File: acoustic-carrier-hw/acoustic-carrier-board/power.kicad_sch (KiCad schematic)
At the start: 71 parts, among them J201 Conn_02x06_Odd_Even, Q201 AO3401A, U201 TPS2121RUX, U202 TLV62569DBV, U203 TLV62569DBV, U204 TLV62569DBV, U205 TLV62569DBV, U206 OPA376xxDBV

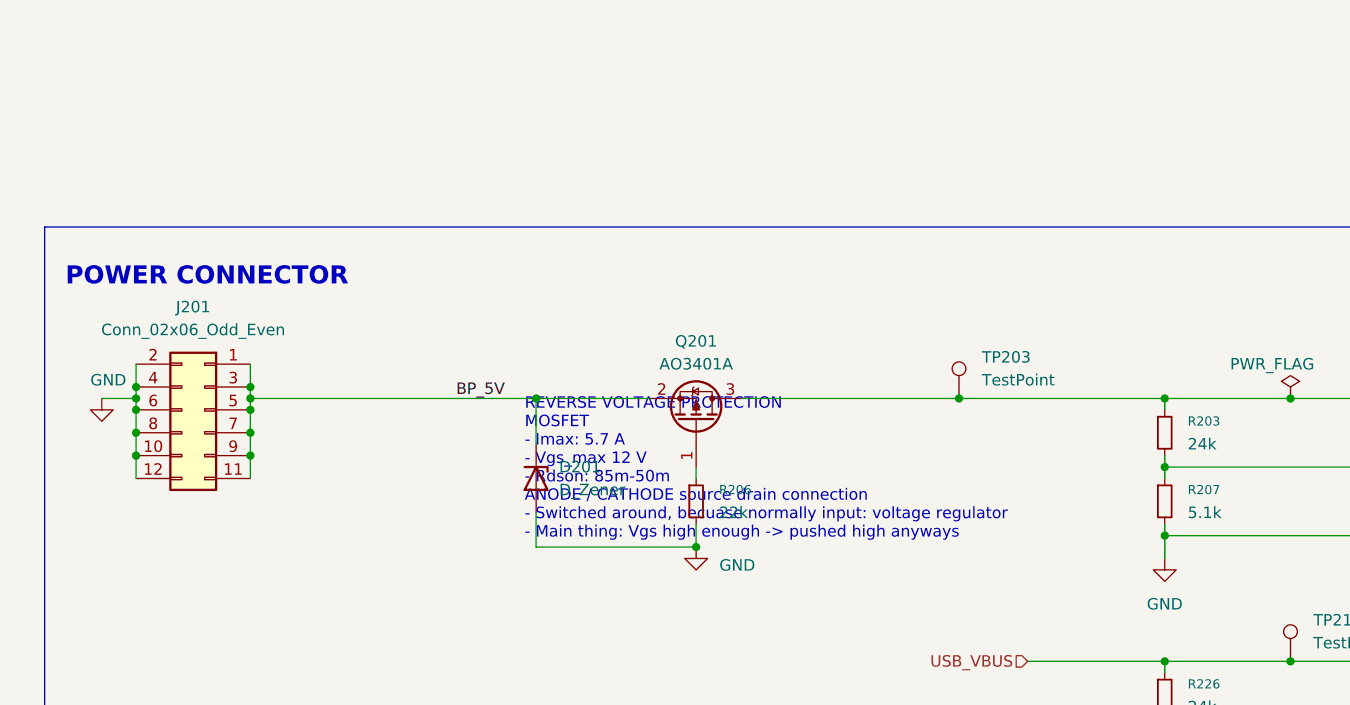
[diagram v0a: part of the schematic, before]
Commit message: [carrier] Routed out signals for board-to-board PTH
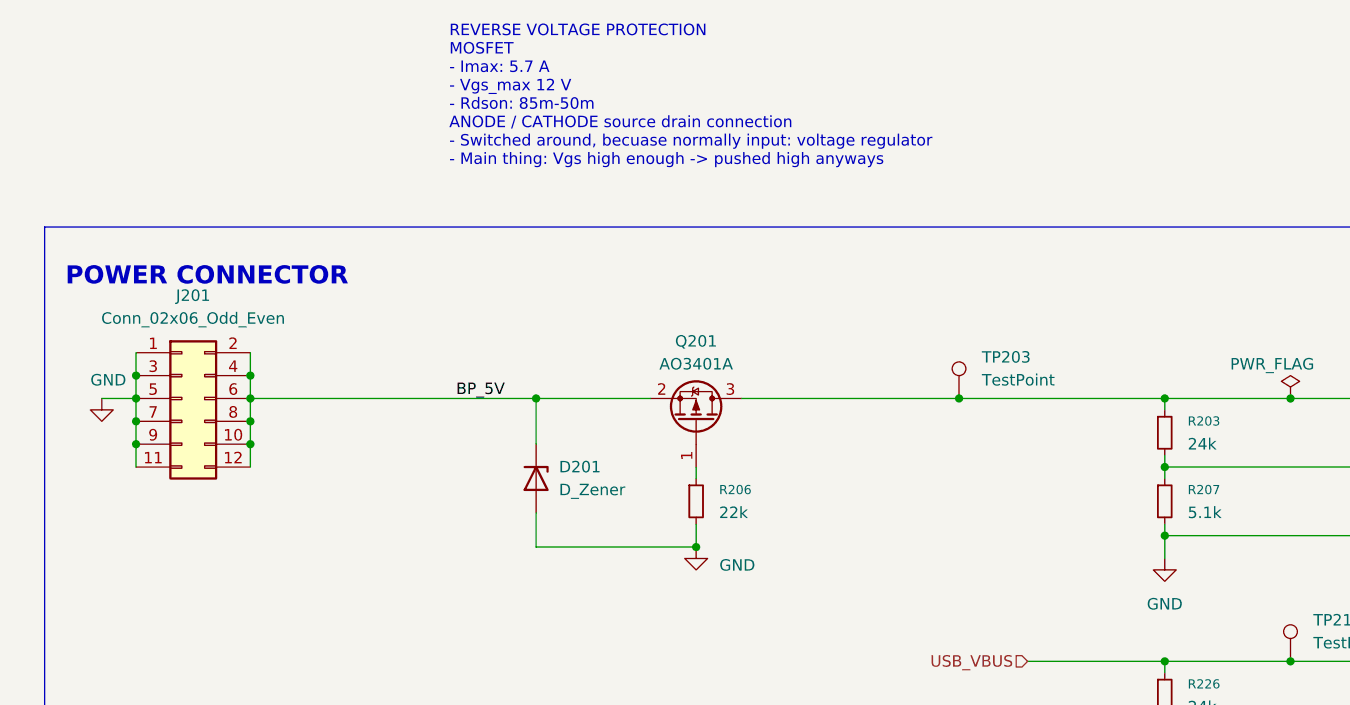
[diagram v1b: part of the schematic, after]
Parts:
- J201: footprint Connector_PinSocket_2.54mm:PinSocket_2x06_P2.54mm_Horizontal -> Connector_PinSocket_2.54mm:PinSocket_2x06_P2.54mm_Vertical; LPN C2897426 -> (none); MPN PM254-2-06-W-8.5 -> (none)
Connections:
- net BP_5V: now also J201.10 (Pin_10), J201.12 (Pin_12), J201.2 (Pin_2), J201.4 (Pin_4), J201.6 (Pin_6), J201.8 (Pin_8); no longer J201.1 (Pin_1), J201.11 (Pin_11), J201.3 (Pin_3), J201.5 (Pin_5), J201.7 (Pin_7), J201.9 (Pin_9)
- net GND: now also J201.1 (Pin_1), J201.11 (Pin_11), J201.3 (Pin_3), J201.5 (Pin_5), J201.7 (Pin_7), J201.9 (Pin_9); no longer J201.10 (Pin_10), J201.12 (Pin_12), J201.2 (Pin_2), J201.4 (Pin_4), J201.6 (Pin_6), J201.8 (Pin_8)

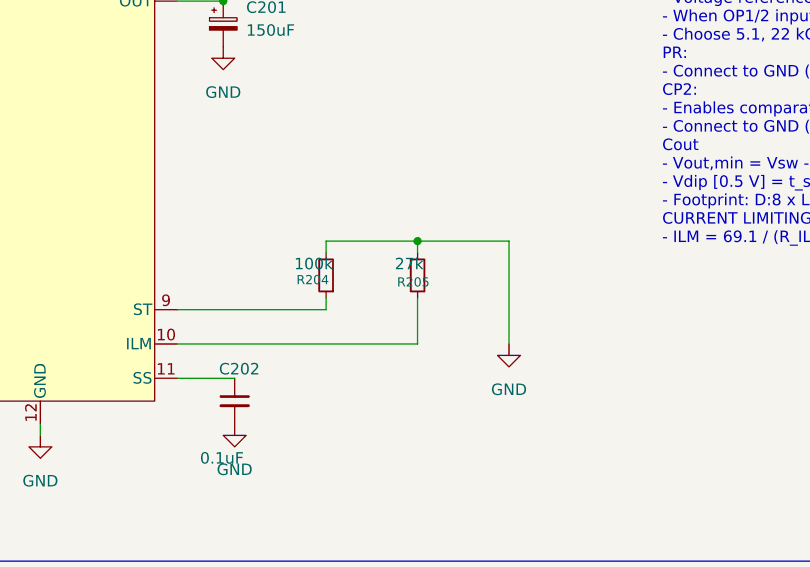
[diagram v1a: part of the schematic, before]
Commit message: [carrier] Changed all vias to (pcheaper) 0.2/0.35 size (next) create basic test-VHDL for clock-signal fanout checks
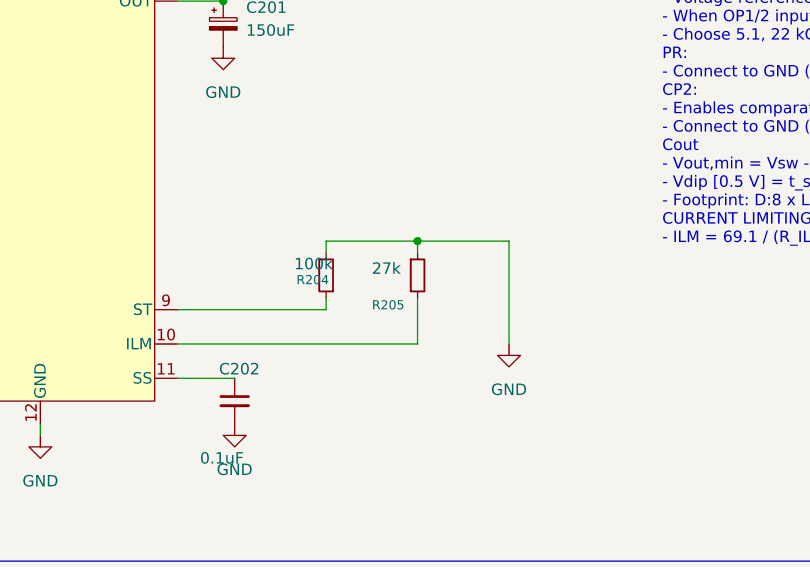
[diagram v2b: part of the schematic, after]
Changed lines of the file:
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@@
 		(dnp no)
 		(property "Reference" "R205"
-			(at 223.774 75.692 0)
+			(at 220.98 78.232 0)
 			(effects
 				(font
@@
 		)
 		(property "Value" "27k"
-			(at 223.52 73.66 0)
+			(at 220.98 74.168 0)
 			(effects
 				(font

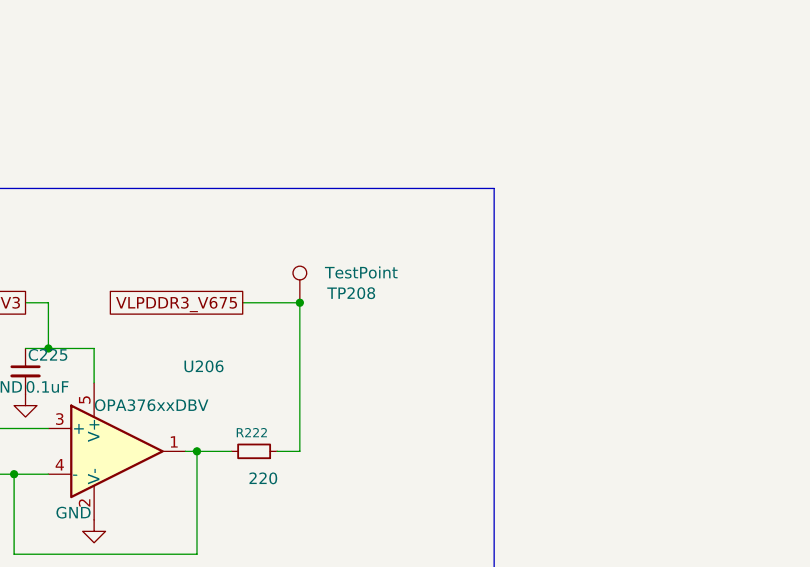
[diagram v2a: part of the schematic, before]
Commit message: [carrier] Added decoupling to LPDDR3 and routed VREF (next) finalize power supply
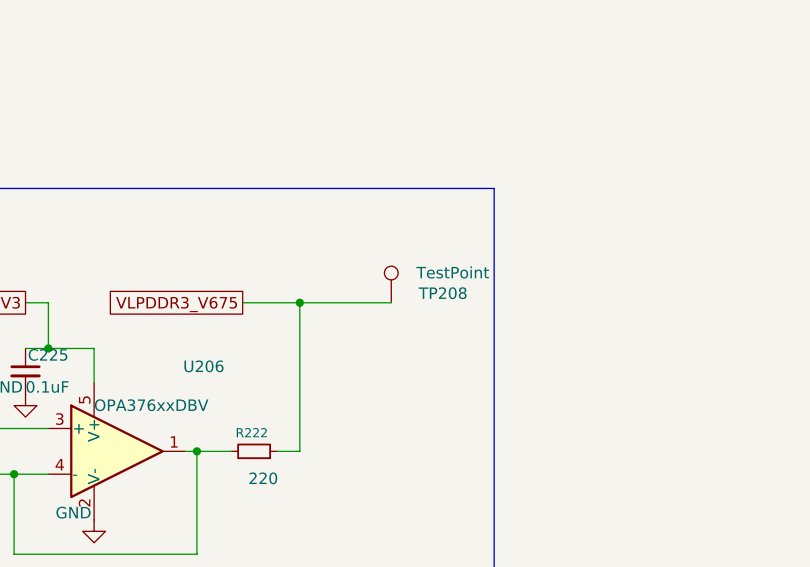
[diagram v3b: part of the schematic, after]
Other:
- moved on the sheet: TP208
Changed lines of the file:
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@@
 	(wire
 		(pts
+			(xy 281.94 237.49) (xy 271.78 237.49)
+		)
+		(stroke
+			(width 0)
+			(type default)
+		)
+	)
+	(wire
+		(pts
 			(xy 215.9 71.12) (xy 215.9 72.39)
 		)
@@
 	(symbol
 		(lib_id "Connector:TestPoint")
-		(at 271.78 237.49 0)
+		(at 281.94 237.49 0)
 		(unit 1)
 		(exclude_from_sim no)
@@
 		(dnp no)
 		(property "Reference" "TP208"
-			(at 274.828 236.474 0)
+			(at 284.988 236.474 0)
 			(effects
 				(font
@@
 		)
 		(property "Value" "TestPoint"
-			(at 274.574 234.188 0)
+			(at 284.734 234.188 0)
 			(effects
 				(font
@@
 		)
 		(property "Footprint" "TestPoint:TestPoint_Loop_D1.80mm_Drill1.0mm_Beaded"
-			(at 276.86 237.49 0)
+			(at 287.02 237.49 0)
 			(effects
 				(font
@@
 		)
 		(property "Datasheet" "~"
-			(at 276.86 237.49 0)
+			(at 287.02 237.49 0)
 			(effects
 				(font
@@
 		)
 		(property "Description" "test point"
-			(at 271.78 237.49 0)
+			(at 281.94 237.49 0)
 			(effects
 				(font

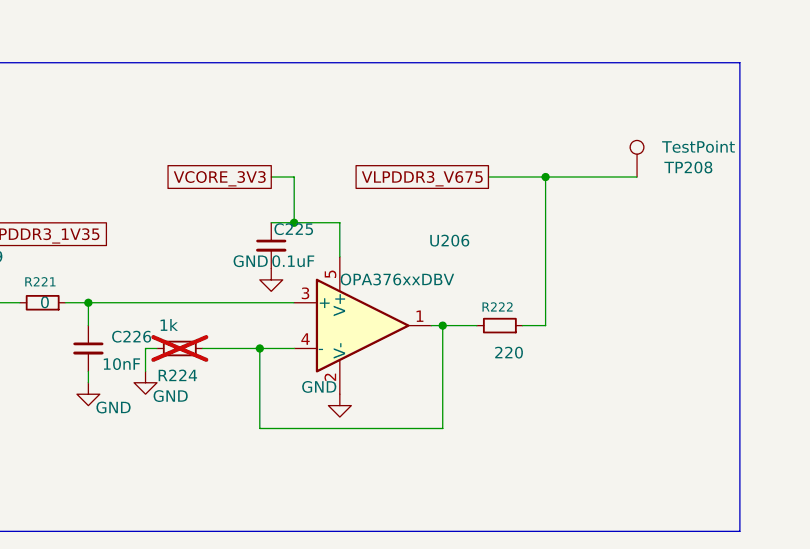
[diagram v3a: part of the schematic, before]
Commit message: [carrier] Further routing, ground plane removal underneath connectors, ..
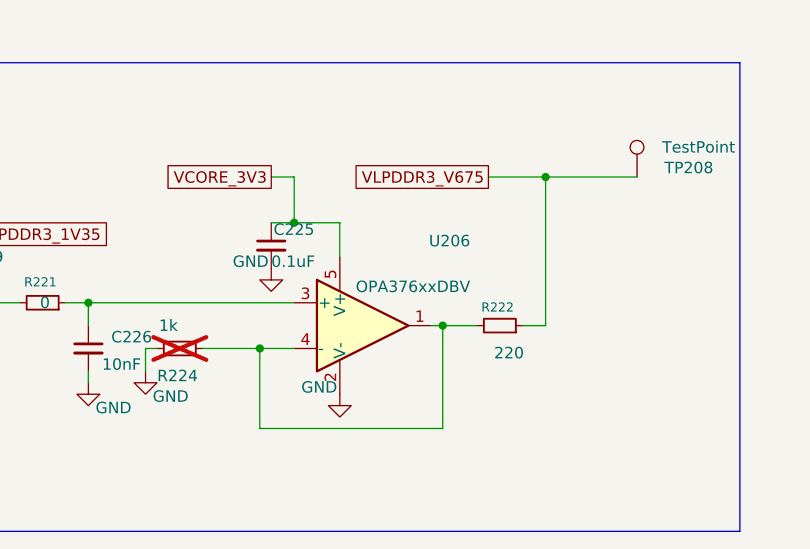
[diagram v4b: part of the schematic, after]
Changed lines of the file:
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@@
 		)
 		(property "Value" "OPA376xxDBV"
-			(at 255.27 248.92 0)
+			(at 257.048 249.682 0)
 			(effects
 				(font

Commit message: [carrier] Added extra decoupling to ADC bias voltage
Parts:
- removed TP203, TP207: TestPoint, TestPoint:TestPoint_Loop_D1.80mm_Drill1.0mm_Beaded, symbol Connector:TestPoint
- TP206: footprint TestPoint:TestPoint_Loop_D1.80mm_Drill1.0mm_Beaded -> TestPoint:TestPoint_Pad_D2.0mm
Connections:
- net +1V2: no longer TP206.1
- net +1V35: no longer TP209.1
- net +3V3: no longer TP205.1
- net VCORE_3V3: now also TP205.1
- net VETH_1V2: now also TP206.1
- net VLPDDR3_1V35: now also TP209.1
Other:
- moved on the sheet: TP205, TP206, TP209

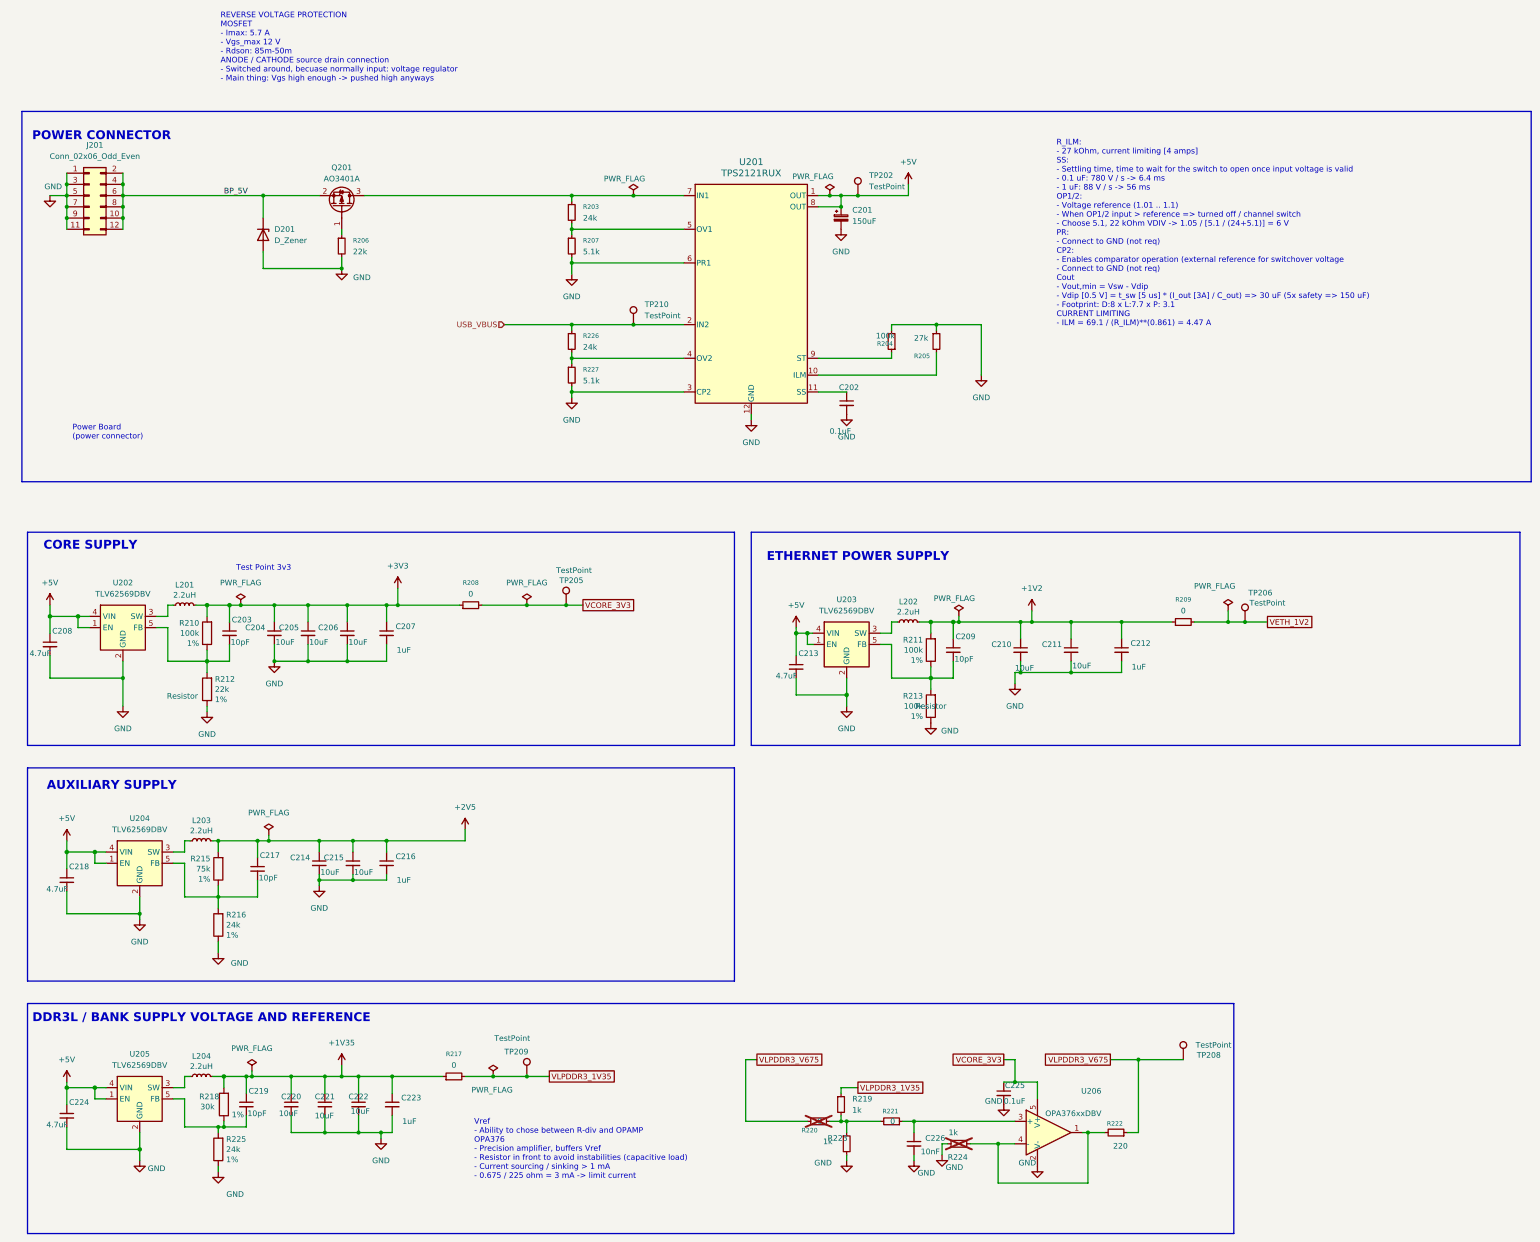
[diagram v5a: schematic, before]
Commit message: [carrier] Added delayed startup + some traces (next) fix the errors inside the DDR3 routing somehow
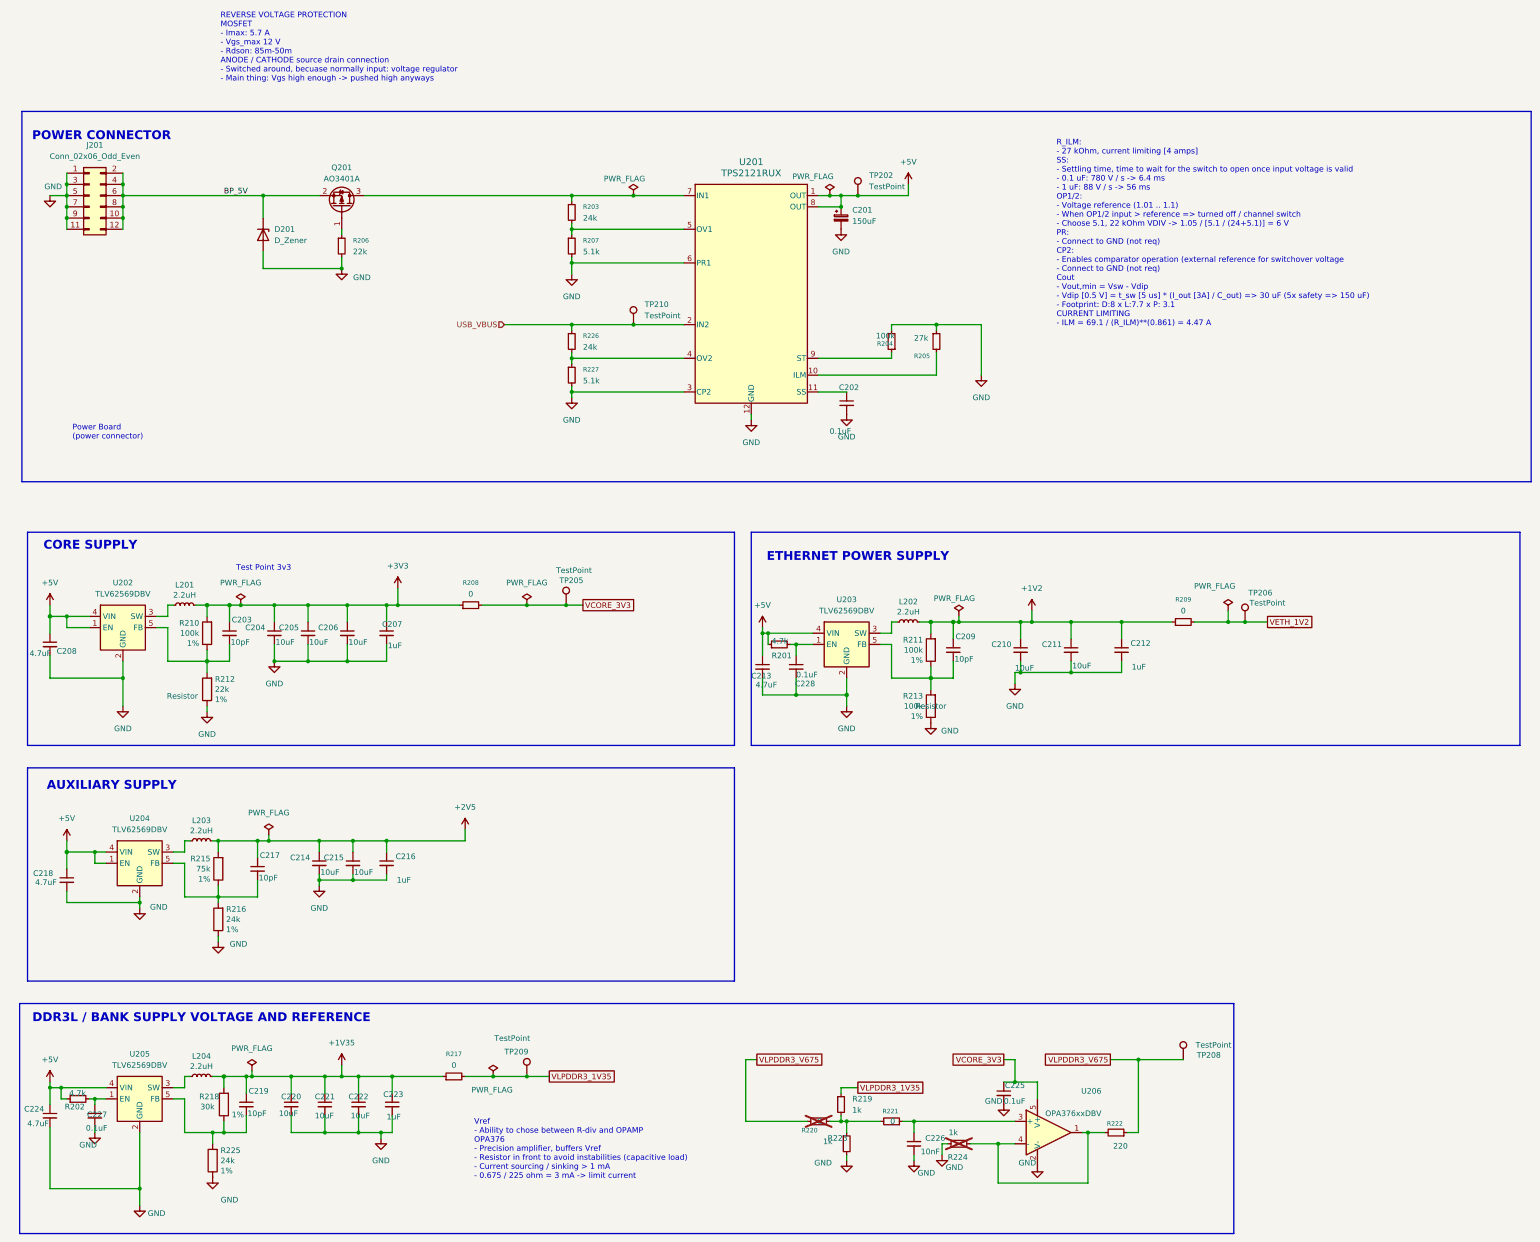
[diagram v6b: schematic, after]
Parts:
- added C227, C228: 0.1uF, Capacitor_SMD:C_0201_0603Metric, symbol Device:C_Small
- added R201, R202: 4.7k, Resistor_SMD:R_0402_1005Metric, symbol Device:R_Small
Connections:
- net +5V: now also R201.1, R202.1; no longer U203.1 (EN), U205.1 (EN)
- net GND: now also C227.2, C228.2
- new net: C228.1, R201.2, U203.1 (EN)
- new net: C227.1, R202.2, U205.1 (EN)
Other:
- moved on the sheet: C213, C224, R216, R225
